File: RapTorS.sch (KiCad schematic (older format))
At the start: 22 parts, among them J1 Molex 48037-2200, J2 TestPoint, J3 TestPoint, J4 TestPoint, J5 TestPoint, J6 TestPoint, U1 PIC16LF1454-I_ML, U2 TLV71333PDBV, U3 E07-M1101S

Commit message: placement second step
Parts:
- removed C5: 100nF, Capacitors_SMD:C_0805, symbol RapTorS-rescue:C-device
- J2: footprint Connectors_TestPoints:Test_Point_Pad_1.5x1.5mm -> Connectors_TestPoints:Test_Point_Pad_d1.5mm
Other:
- note added: "No capacitor in input, because there is already C2"
- moved on the sheet: C6, U2
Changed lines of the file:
@@
-$EndComp
-$Comp
-L RapTorS-rescue:C-device C5
-U 1 1 5B62F7D7
-P 1500 3800
-F 0 "C5" H 1615 3846 50  0000 L CNN
-F 1 "100nF" H 1615 3755 50  0000 L CNN
-F 2 "Capacitors_SMD:C_0805" H 1538 3650 50  0001 C CNN
-F 3 "" H 1500 3800 50  0001 C CNN
-	1    1500 3800
-	1    0    0    -1
 $EndComp
 $Comp
@@
 L RapTorS-rescue:TLV71333PDBV-regul U2
 U 1 1 5B6396D9
-P 2300 3600
-F 0 "U2" H 2300 3942 50  0000 C CNN
-F 1 "TLV71333PDBV" H 2300 3851 50  0000 C CNN
-F 2 "TO_SOT_Packages_SMD:SOT-23-5" H 2300 3925 50  0001 C CIN
-F 3 "http://www.ti.com/lit/ds/symlink/tlv713p.pdf" H 2300 3600 50  0001 C CNN
-	1    2300 3600
+P 2300 3400
+F 0 "U2" H 2300 3742 50  0000 C CNN
+F 1 "TLV71333PDBV" H 2300 3651 50  0000 C CNN
+F 2 "TO_SOT_Packages_SMD:SOT-23-5" H 2300 3725 50  0001 C CIN
+F 3 "http://www.ti.com/lit/ds/symlink/tlv713p.pdf" H 2300 3400 50  0001 C CNN
+	1    2300 3400
 	1    0    0    -1
 $EndComp
@@
 L power:GND #PWR017
 U 1 1 5B68188F
-P 2300 4150
-F 0 "#PWR017" H 2300 3900 50  0001 C CNN
-F 1 "GND" H 2305 3977 50  0000 C CNN
-F 2 "" H 2300 4150 50  0001 C CNN
-F 3 "" H 2300 4150 50  0001 C CNN
-	1    2300 4150
-	1    0    0    -1
-$EndComp
-$Comp
-L power:GND #PWR016
-U 1 1 5B6818B6
-P 1500 4150
-F 0 "#PWR016" H 1500 3900 50  0001 C CNN
-F 1 "GND" H 1505 3977 50  0000 C CNN
-F 2 "" H 1500 4150 50  0001 C CNN
-F 3 "" H 1500 4150 50  0001 C CNN
-	1    1500 4150
-	1    0    0    -1
-$EndComp
-Wire Wire Line
-	1500 4150 1500 3950
-Wire Wire Line
-	1500 3500 1900 3500
-Wire Wire Line
-	2000 3600 1900 3600
-Wire Wire Line
-	1900 3600 1900 3500
-Connection ~ 1900 3500
-Wire Wire Line
-	1900 3500 2000 3500
-Wire Wire Line
-	1500 3500 1500 3650
-Wire Wire Line
-	2300 4150 2300 3900
+P 2300 3950
+F 0 "#PWR017" H 2300 3700 50  0001 C CNN
+F 1 "GND" H 2305 3777 50  0000 C CNN
+F 2 "" H 2300 3950 50  0001 C CNN
+F 3 "" H 2300 3950 50  0001 C CNN
+	1    2300 3950
+	1    0    0    -1
+$EndComp
+Wire Wire Line
+	1500 3300 1900 3300
+Wire Wire Line
+	2000 3400 1900 3400
+Wire Wire Line
+	1900 3400 1900 3300
+Connection ~ 1900 3300
+Wire Wire Line
+	1900 3300 2000 3300
+Wire Wire Line
+	2300 3950 2300 3700
 $Comp
 L power:+5V #PWR012
 U 1 1 5B683BB0
-P 1500 3400
-F 0 "#PWR012" H 1500 3250 50  0001 C CNN
-F 1 "+5V" H 1515 3573 50  0000 C CNN
-F 2 "" H 1500 3400 50  0001 C CNN
-F 3 "" H 1500 3400 50  0001 C CNN
-	1    1500 3400
-	1    0    0    -1
-$EndComp
-Wire Wire Line
-	1500 3500 1500 3400
-Connection ~ 1500 3500
+P 1500 3200
+F 0 "#PWR012" H 1500 3050 50  0001 C CNN
+F 1 "+5V" H 1515 3373 50  0000 C CNN
+F 2 "" H 1500 3200 50  0001 C CNN
+F 3 "" H 1500 3200 50  0001 C CNN
+	1    1500 3200
+	1    0    0    -1
+$EndComp
+Wire Wire Line
+	1500 3300 1500 3200
 $Comp
 L RapTorS-rescue:C-device C6
 U 1 1 5B684462
-P 2750 3800
-F 0 "C6" H 2865 3846 50  0000 L CNN
-F 1 "100nF" H 2865 3755 50  0000 L CNN
-F 2 "Capacitors_SMD:C_0805" H 2788 3650 50  0001 C CNN
-F 3 "" H 2750 3800 50  0001 C CNN
-	1    2750 3800
-	1    0    0    -1
-$EndComp
-Wire Wire Line
-	2600 3500 2750 3500
-Wire Wire Line
-	2750 3500 2750 3650
+P 2750 3600
+F 0 "C6" H 2865 3646 50  0000 L CNN
+F 1 "100nF" H 2865 3555 50  0000 L CNN
+F 2 "Capacitors_SMD:C_0805" H 2788 3450 50  0001 C CNN
+F 3 "" H 2750 3600 50  0001 C CNN
+	1    2750 3600
+	1    0    0    -1
+$EndComp
+Wire Wire Line
+	2600 3300 2750 3300
+Wire Wire Line
+	2750 3300 2750 3450
 $Comp
 L power:GND #PWR018
 U 1 1 5B684DFE
-P 2750 4150
-F 0 "#PWR018" H 2750 3900 50  0001 C CNN
-F 1 "GND" H 2755 3977 50  0000 C CNN
-F 2 "" H 2750 4150 50  0001 C CNN
-F 3 "" H 2750 4150 50  0001 C CNN
-	1    2750 4150
-	1    0    0    -1
-$EndComp
-Wire Wire Line
-	2750 4150 2750 3950
+P 2750 3950
+F 0 "#PWR018" H 2750 3700 50  0001 C CNN
+F 1 "GND" H 2755 3777 50  0000 C CNN
+F 2 "" H 2750 3950 50  0001 C CNN
+F 3 "" H 2750 3950 50  0001 C CNN
+	1    2750 3950
+	1    0    0    -1
+$EndComp
+Wire Wire Line
+	2750 3950 2750 3750
 $Comp
 L power:+3V3 #PWR013
 U 1 1 5B685845
-P 2750 3400
-F 0 "#PWR013" H 2750 3250 50  0001 C CNN
-F 1 "+3V3" H 2765 3573 50  0000 C CNN
-F 2 "" H 2750 3400 50  0001 C CNN
-F 3 "" H 2750 3400 50  0001 C CNN
-	1    2750 3400
-	1    0    0    -1
-$EndComp
-Connection ~ 2750 3500
-Wire Wire Line
-	2750 3400 2750 3500
+P 2750 3200
+F 0 "#PWR013" H 2750 3050 50  0001 C CNN
+F 1 "+3V3" H 2765 3373 50  0000 C CNN
+F 2 "" H 2750 3200 50  0001 C CNN
+F 3 "" H 2750 3200 50  0001 C CNN
+	1    2750 3200
+	1    0    0    -1
+$EndComp
+Connection ~ 2750 3300
+Wire Wire Line
+	2750 3200 2750 3300
 Wire Notes Line
 	1000 2800 3700 2800
@@
 F 0 "J2" V 5700 3787 50  0000 L CNN
 F 1 "TestPoint" V 5745 3788 50  0001 L CNN
-F 2 "Connectors_TestPoints:Test_Point_Pad_1.5x1.5mm" H 5900 3600 50  0001 C CNN
+F 2 "Connectors_TestPoints:Test_Point_Pad_d1.5mm" H 5900 3600 50  0001 C CNN
 F 3 "~" H 5900 3600 50  0001 C CNN
 	1    5700 3600
@@
 Wire Notes Line
 	1000 800  3900 800
+Text Notes 1050 4450 0    50   ~ 0
+No capacitor in input, because there is already C2
 $EndSCHEMATC

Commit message: change C3 to ceramic, in order to fit in the case
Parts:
- removed C3: 4.7uF, Capacitors_SMD:CP_Elec_4x4.5, symbol RapTorS-rescue:CP1-device
- added C3: 4.7uF, Capacitors_SMD:C_0805, symbol RapTorS-rescue:C-device
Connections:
- net +5V: now also C3.1
- net GND: now also C3.2
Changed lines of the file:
@@
 	1    0    0    -1
-$EndComp
-$Comp
-L RapTorS-rescue:CP1-device C3
-U 1 1 5B63038C
-P 3550 1550
-F 0 "C3" H 3435 1596 50  0000 R CNN
-F 1 "4.7uF" H 3435 1505 50  0000 R CNN
-F 2 "Capacitors_SMD:CP_Elec_4x4.5" H 3550 1550 50  0001 C CNN
-F 3 "" H 3550 1550 50  0001 C CNN
-	1    3550 1550
-	-1   0    0    -1
 $EndComp
 Wire Wire Line
@@
 Text Notes 1050 4450 0    50   ~ 0
 No capacitor in input, because there is already C2
+$Comp
+L RapTorS-rescue:C-device C3
+U 1 1 5B887802
+P 3550 1550
+F 0 "C3" H 3665 1596 50  0000 L CNN
+F 1 "4.7uF" H 3665 1505 50  0000 L CNN
+F 2 "Capacitors_SMD:C_0805" H 3588 1400 50  0001 C CNN
+F 3 "" H 3550 1550 50  0001 C CNN
+	1    3550 1550
+	1    0    0    -1
+$EndComp
 $EndSCHEMATC

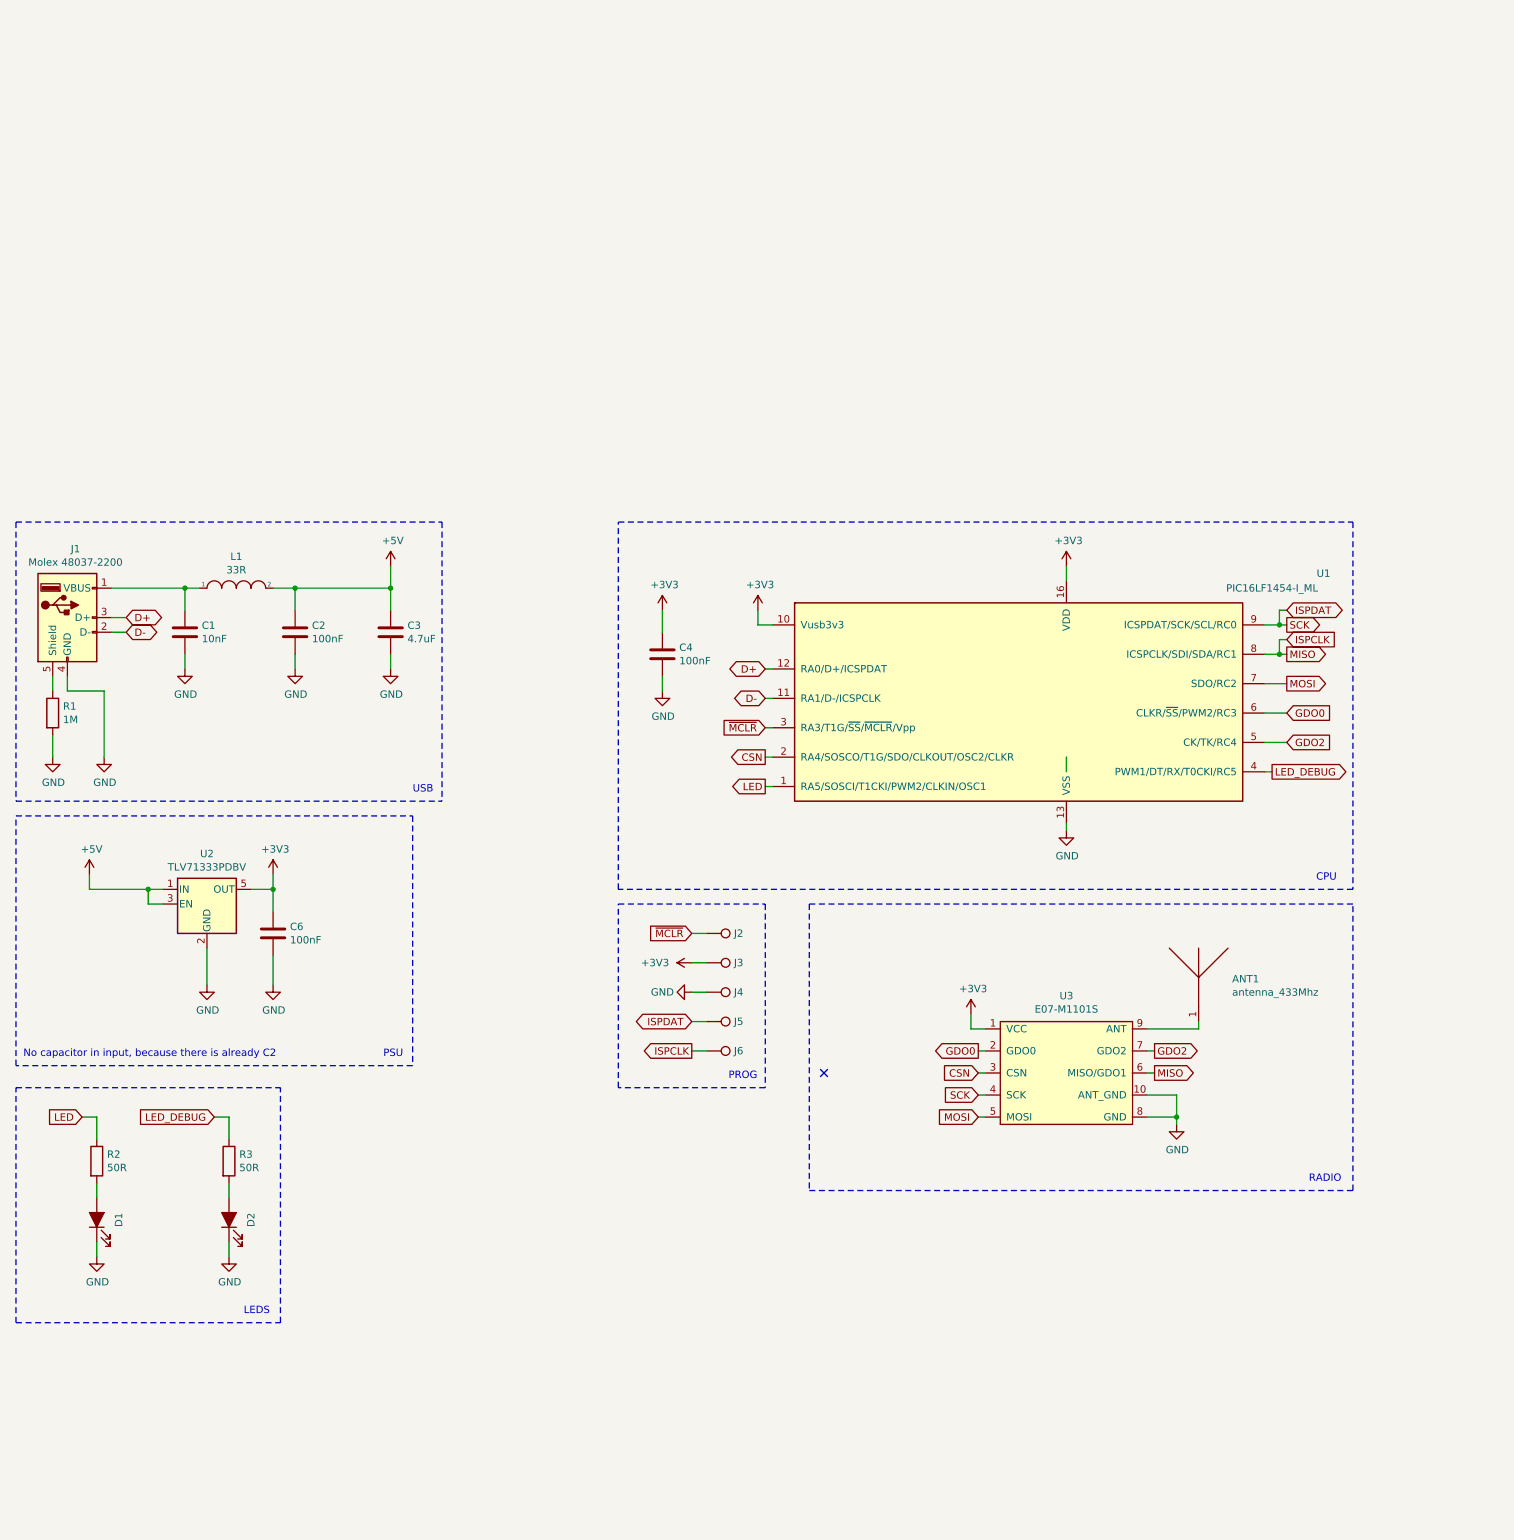
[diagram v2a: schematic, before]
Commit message: add EFM32HG308 lib - add new uController on schematic
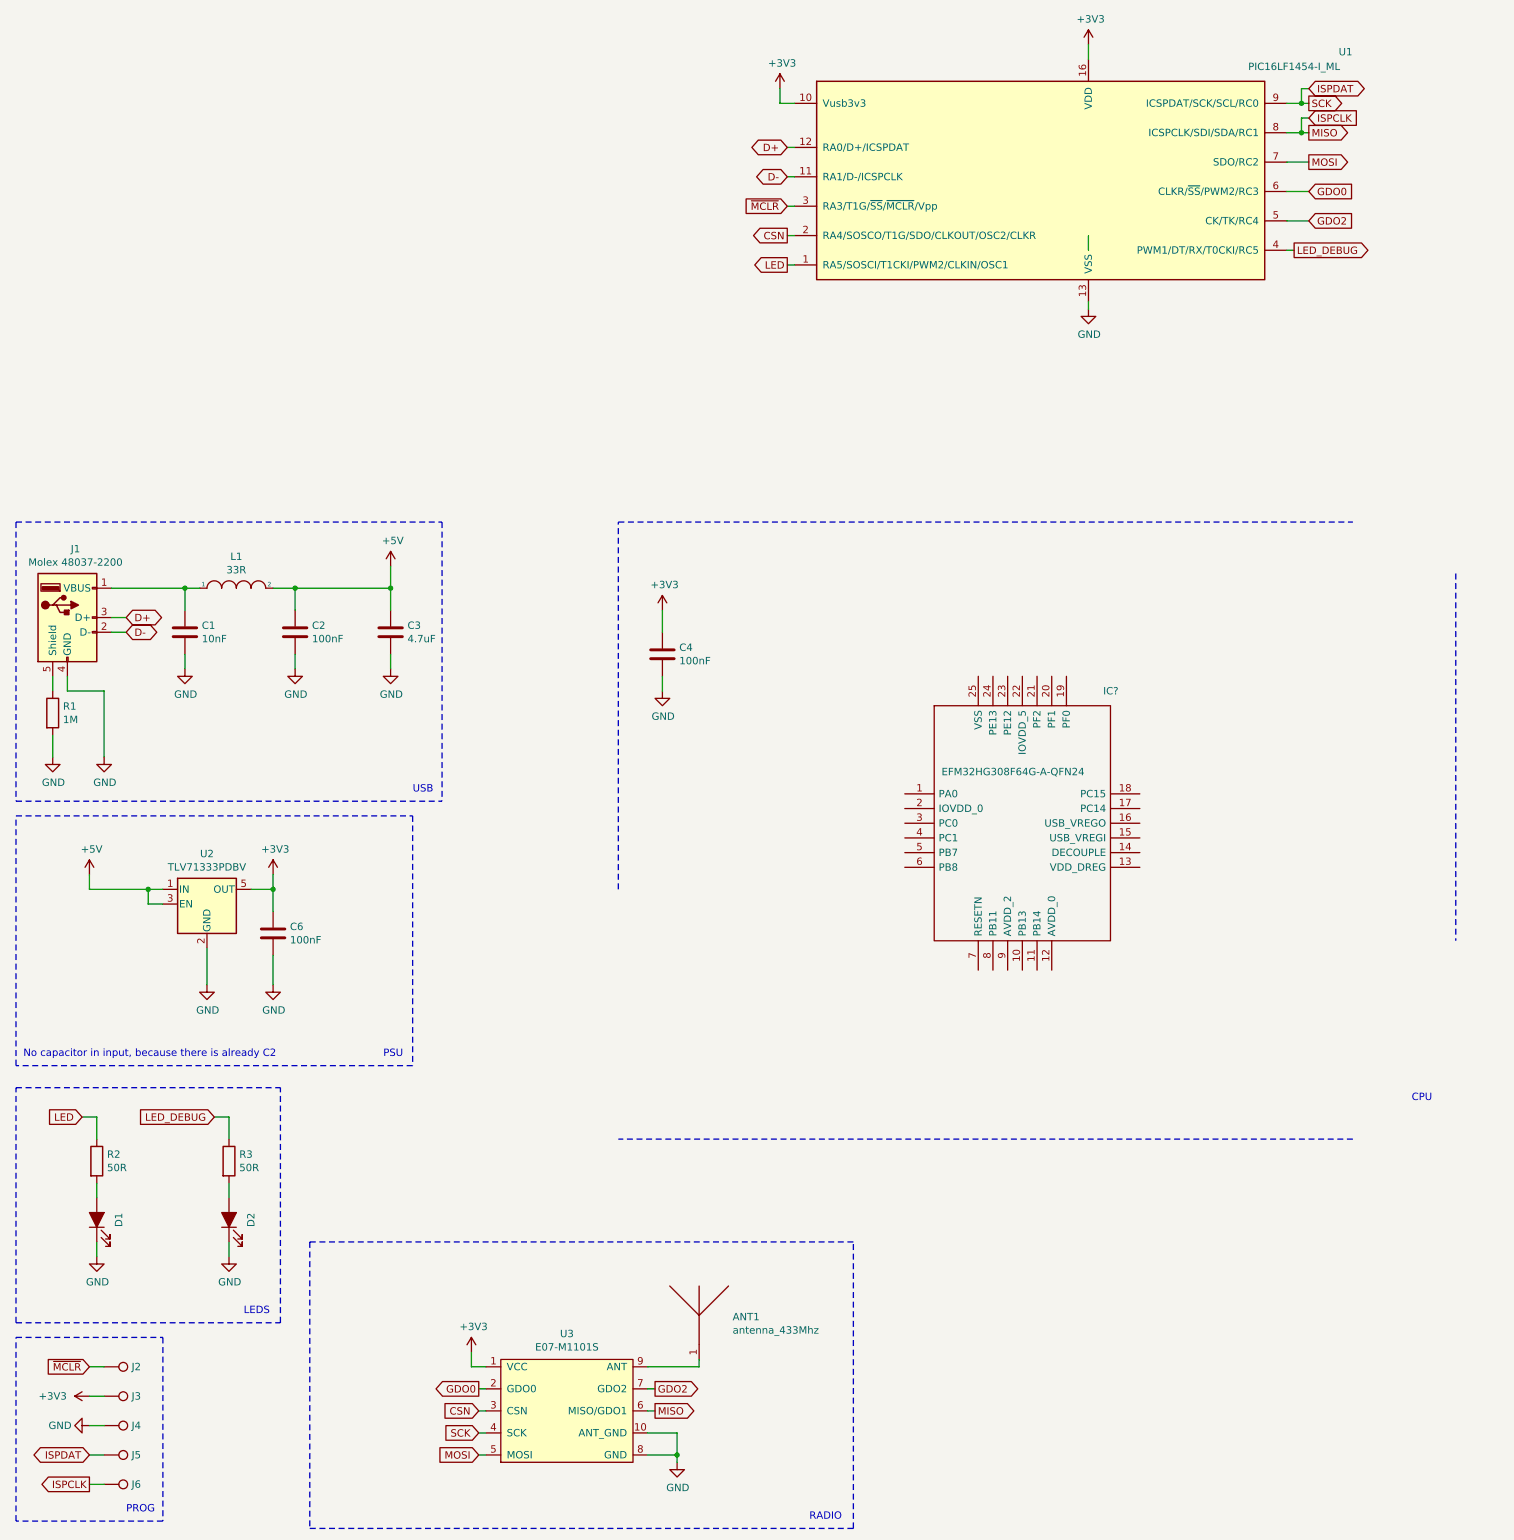
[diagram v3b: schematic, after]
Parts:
- added IC?: EFM32HG308F64G-A-QFN24, QFN65P500X500X90-25N, symbol EFM32HG308F64G-A-QFN24:EFM32HG308F64G-A-QFN24
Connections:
- no-connect marks 1 -> 0
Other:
- moved on the sheet: ANT1, J2, J3, J4, J5, J6, U1, U3

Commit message: routing completed
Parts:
- removed D2: LED_ALT, LEDs:LED_0805, symbol RapTorS-rescue:LED_ALT-device
- removed R3: 50R, Resistors_SMD:R_0805, symbol RapTorS-rescue:R-device
- removed U1: PIC16LF1454-I_ML, Housings_DFN_QFN:QFN-16-1EP_4x4mm_Pitch0.65mm, symbol RapTorS-rescue:PIC16(L)F1454-I_ML-MCU_Microchip_PIC16
- added C5, C7, C8, C9: 1uF, Capacitors_SMD:C_0603, symbol RapTorS-rescue:C-device
- added R4, R5: 15R, Resistors_SMD:R_0603, symbol RapTorS-rescue:R-device
- C1, C2, C3, C4, C6: footprint Capacitors_SMD:C_0805 -> Capacitors_SMD:C_0603
- IC1: renamed from IC?; footprint QFN65P500X500X90-25N -> Housings_DFN_QFN:QFN-24-1EP_5x5mm_Pitch0.65mm
- L1: footprint Inductors_SMD:L_0805 -> Inductors_SMD:L_0603
- R1, R2: footprint Resistors_SMD:R_0805 -> Resistors_SMD:R_0603
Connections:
- net labels added: SWCLK, SWDIO, ~RESET
- net labels removed: ISPCLK, ISPDAT, ~MCLR
- wire segments 79 -> 93
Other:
- note added: "SDA"
- moved on the sheet: C4
